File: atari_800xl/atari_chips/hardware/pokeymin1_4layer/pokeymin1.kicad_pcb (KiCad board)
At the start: 4 copper layers, 17 x 50.8 mm, 101 parts, among them J1 Conn_02x03_Odd_Even, U1 TSV851ICT

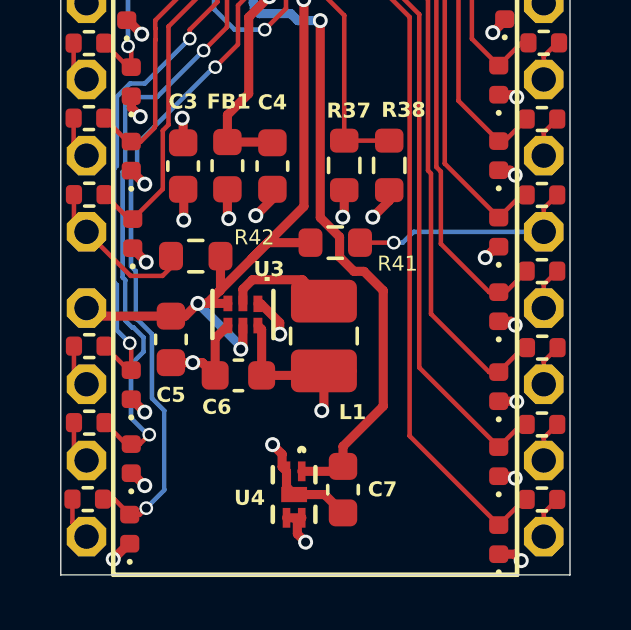
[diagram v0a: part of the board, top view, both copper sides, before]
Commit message: Change regulator to a linear one that works with the io pin protection scheme
git-svn-id: svn+ssh://192.168.0.3/home/svnfpga/repo/trunk@1479 d6161ac3-aae1-4d52-9b05-ea9ac36b53d3
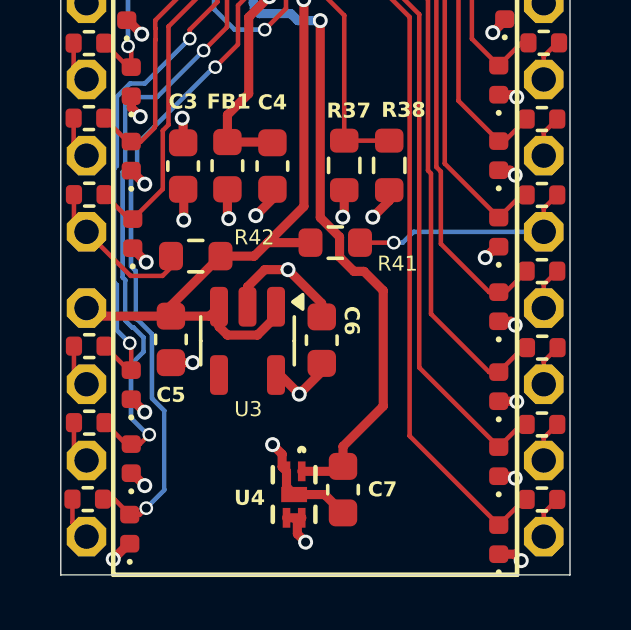
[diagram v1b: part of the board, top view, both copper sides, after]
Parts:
- removed L1: L, Inductor_SMD:L_1008_2520Metric_Pad1.43x2.20mm_HandSolder
- U3: value ~ -> TLV75533PDBV; footprint max10:DRY6 -> Package_TO_SOT_SMD:SOT-23-5
- moved C6 3.02 mm to (27.6, 63.6), turned to 90 degrees
- moved U3 0.89 mm to (25.1, 63.7)
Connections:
- U3 pad 1: GND -> +5V
- U3 pad 2: Net-(U3-SW) -> GND
- U3 pad 4: GND -> unconnected-(U3-NC-Pad4)
- U3 pad 5: +5V -> +3.3V
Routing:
- net +3.3V: track 57.0 -> 53.1 mm
- net Net-(U3-SW): track 3.60 -> 0.00 mm
- net +5V: track 52.9 -> 52.2 mm, vias 4 -> 2
